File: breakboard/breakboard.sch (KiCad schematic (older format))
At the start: 2 parts

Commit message: few tracks
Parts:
- added P23, P24, P25, P48, P50, P51, P52, P81, P85, P86, P87, P88, P? (x6): CONN_1, symbol CONN_1
- gave numbers to parts that had none: 1
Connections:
- wire segments 0 -> 20
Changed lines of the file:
@@
-EESchema Schematic File Version 2  date Sun 14 Oct 2012 05:05:43 PM CEST
+EESchema Schematic File Version 2  date Tue 16 Oct 2012 02:37:21 PM CEST
 LIBS:power
 LIBS:device
@@
 LIBS:contrib
 LIBS:valves
-LIBS:motronic
+LIBS:motronic88
 LIBS:breakboard-cache
 EELAYER 25  0
@@
 Sheet 1 1
 Title ""
-Date "14 oct 2012"
+Date "16 oct 2012"
 Rev ""
 Comp ""
@@
 Comment4 ""
 $EndDescr
+Wire Wire Line
+	5100 1750 5100 1265
+Wire Wire Line
+	3950 2800 4700 2800
+Wire Wire Line
+	4700 2800 4700 1315
+Wire Wire Line
+	3950 2700 4900 2700
+Wire Wire Line
+	4900 2700 4900 1315
+Wire Wire Line
+	3950 2500 4850 2500
+Wire Wire Line
+	4850 2500 4850 1315
+Wire Wire Line
+	4750 1750 4750 1615
+Wire Wire Line
+	4250 1750 4250 1615
+Wire Wire Line
+	4050 1750 4050 1615
+Wire Wire Line
+	4150 1615 4150 1750
+Wire Wire Line
+	4350 1615 4350 1750
+Wire Wire Line
+	4800 1315 4800 2900
+Wire Wire Line
+	4800 2900 3950 2900
+Wire Wire Line
+	4650 1315 4650 2400
+Wire Wire Line
+	4650 2400 3950 2400
+Wire Wire Line
+	4750 1315 4750 1350
+Wire Wire Line
+	4750 1350 4600 1350
+Wire Wire Line
+	4600 1350 4600 2600
+Wire Wire Line
+	4600 2600 3950 2600
+$Comp
+L CONN_1 P48
+U 1 1 507D5328
+P 5100 1900
+F 0 "P48" H 5180 1900 40  0000 L CNN
+F 1 "CONN_1" H 5100 1955 30  0001 C CNN
+	1    5100 1900
+	0    1    1    0
+$EndComp
+$Comp
+L CONN_1 P81
+U 1 1 507D5152
+P 4750 1900
+F 0 "P81" H 4830 1900 40  0000 L CNN
+F 1 "CONN_1" H 4750 1955 30  0001 C CNN
+	1    4750 1900
+	0    1    1    0
+$EndComp
+$Comp
+L CONN_1 P85
+U 1 1 507D514F
+P 4350 1900
+F 0 "P85" H 4430 1900 40  0000 L CNN
+F 1 "CONN_1" H 4350 1955 30  0001 C CNN
+	1    4350 1900
+	0    1    1    0
+$EndComp
+$Comp
+L CONN_1 P?
+U 1 1 507D511B
+P 3450 2900
+F 0 "P?" H 3530 2900 40  0001 L CNN
+F 1 "CONN_1" H 3450 2955 30  0001 C CNN
+	1    3450 2900
+	1    0    0    -1
+$EndComp
+$Comp
+L CONN_1 P?
+U 1 1 507D5119
+P 3450 2800
+F 0 "P?" H 3530 2800 40  0001 L CNN
+F 1 "CONN_1" H 3450 2855 30  0001 C CNN
+	1    3450 2800
+	1    0    0    -1
+$EndComp
+$Comp
+L CONN_1 P?
+U 1 1 507D5118
+P 3450 2700
+F 0 "P?" H 3530 2700 40  0001 L CNN
+F 1 "CONN_1" H 3450 2755 30  0001 C CNN
+	1    3450 2700
+	1    0    0    -1
+$EndComp
+$Comp
+L CONN_1 P?
+U 1 1 507D5116
+P 3450 2600
+F 0 "P?" H 3530 2600 40  0001 L CNN
+F 1 "CONN_1" H 3450 2655 30  0001 C CNN
+	1    3450 2600
+	1    0    0    -1
+$EndComp
+$Comp
+L CONN_1 P51
+U 1 1 507D5114
+P 3800 2900
+F 0 "P51" H 3880 2900 40  0000 L CNN
+F 1 "CONN_1" H 3800 2955 30  0001 C CNN
+	1    3800 2900
+	-1   0    0    1
+$EndComp
+$Comp
+L CONN_1 P52
+U 1 1 507D5111
+P 3800 2800
+F 0 "P52" H 3880 2800 40  0000 L CNN
+F 1 "CONN_1" H 3800 2855 30  0001 C CNN
+	1    3800 2800
+	-1   0    0    1
+$EndComp
+$Comp
+L CONN_1 P50
+U 1 1 507D510F
+P 3800 2700
+F 0 "P50" H 3880 2700 40  0000 L CNN
+F 1 "CONN_1" H 3800 2755 30  0001 C CNN
+	1    3800 2700
+	-1   0    0    1
+$EndComp
+$Comp
+L CONN_1 P24
+U 1 1 507D510C
+P 3800 2600
+F 0 "P24" H 3880 2600 40  0000 L CNN
+F 1 "CONN_1" H 3800 2655 30  0001 C CNN
+	1    3800 2600
+	-1   0    0    1
+$EndComp
+$Comp
+L CONN_1 P23
+U 1 1 507D50D7
+P 3800 2500
+F 0 "P23" H 3880 2500 40  0000 L CNN
+F 1 "CONN_1" H 3800 2555 30  0001 C CNN
+	1    3800 2500
+	-1   0    0    1
+$EndComp
+$Comp
+L CONN_1 P?
+U 1 1 507D50D3
+P 3450 2500
+F 0 "P?" H 3530 2500 40  0001 L CNN
+F 1 "CONN_1" H 3450 2555 30  0001 C CNN
+	1    3450 2500
+	1    0    0    -1
+$EndComp
+$Comp
+L CONN_1 P25
+U 1 1 507D50C2
+P 3800 2400
+F 0 "P25" H 3880 2400 40  0000 L CNN
+F 1 "CONN_1" H 3800 2455 30  0001 C CNN
+	1    3800 2400
+	-1   0    0    1
+$EndComp
+$Comp
+L CONN_1 P?
+U 1 1 507D50BD
+P 3450 2400
+F 0 "P?" H 3530 2400 40  0001 L CNN
+F 1 "CONN_1" H 3450 2455 30  0001 C CNN
+	1    3450 2400
+	1    0    0    -1
+$EndComp
+$Comp
+L CONN_1 P86
+U 1 1 507D5092
+P 4250 1900
+F 0 "P86" H 4330 1900 40  0000 L CNN
+F 1 "CONN_1" H 4250 1955 30  0001 C CNN
+	1    4250 1900
+	0    1    1    0
+$EndComp
+$Comp
+L CONN_1 P87
+U 1 1 507D508E
+P 4150 1900
+F 0 "P87" H 4230 1900 40  0000 L CNN
+F 1 "CONN_1" H 4150 1955 30  0001 C CNN
+	1    4150 1900
+	0    1    1    0
+$EndComp
+$Comp
+L CONN_1 P88
+U 1 1 507D507A
+P 4050 1900
+F 0 "P88" H 4130 1900 40  0000 L CNN
+F 1 "CONN_1" H 4050 1955 30  0001 C CNN
+	1    4050 1900
+	0    1    1    0
+$EndComp
 $Comp
 L DB37 J?
 U 1 1 507A558A
 P 5650 7000
-F 0 "J?" H 5750 8900 70  0000 C CNN
+F 0 "J?" H 5750 8900 70  0001 C CNN
 F 1 "DB37" H 5600 5050 70  0000 C CNN
 	1    5650 7000
@@
 $EndComp
 $Comp
-L MOTRONIC88 J?
+L MOTRONIC88 J1
 U 1 1 507A5548
 P 4050 1500
-F 0 "J?" H 4130 1500 40  0000 L CNN
+F 0 "J1" H 4130 1500 40  0001 L CNN
 F 1 "MOTRONIC88" H 4050 1555 30  0001 C CNN
 	1    4050 1500

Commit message: wiring
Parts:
- removed P23, P24, P25, P50, P51, P52, P? (x6): CONN_1, symbol CONN_1
- added F1: 2A, symbol FUSE
- added F2: 20A, symbol FUSE
- added JP23, JP24, JP25, JP3, JP4, JP5, JP50, JP51, JP52: JUMPER, symbol JUMPER
- added P11, P13, P14, P16, P17, P36, P41, P44, P60, P64, P65, P73, P8: CONN_1, symbol CONN_1
- added R1, R2, R3, R4, R5, R6: 680, symbol R
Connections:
- wire segments 20 -> 103
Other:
- moved on the sheet: P48, P81, P85, P86, P87, P88

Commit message: idle board/main relay
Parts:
- added +12V, +12V?, FIDLE, ISV1, ISV2: CONN_1, symbol CONN_1
- added D? (x3): 1N4001, symbol DIODE
- added Q1, Q2, Q3, Q4, Q5, Q6: ISL9V5036P3, symbol IGBT
- added Q? (x2): IRFIZ34N, symbol MOSFET_N
- added Q? (x3): PN2222A, symbol NPN
- added R? (x2): 22, symbol R
- added R? (x3): 1k, symbol R
- added R?: 10k, symbol R
- added R? (x2): 22k, symbol R
- added R?: 4.7k, symbol R
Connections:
- net labels added: GND
- wire segments 103 -> 199
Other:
- moved on the sheet: F2

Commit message: gna
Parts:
- added D?: 1N4001, symbol DIODE
- added Q?: PN2222A, symbol NPN
- added R?: 1k, symbol R
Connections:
- net GND: now also F2.2, J1.28, J1.34, J1.43, J1.6, J1.68, J1.71, J?.1, J?.15, J?.16, J?.17, J?.18, J?.19, J?.2, Q1.3 (E), Q2.3 (E), Q3.3 (E), Q4.3 (E), Q5.3 (E), Q6.3 (E), Q?.1 (E)
- net at D?.2 (K), J1.26: now also D?.2 (K)
- net at J1.37: now also D?.1 (A), Q?.3 (C)
- net at J1.56, R?.2: now also R?.2
- net at J1.70: now also J?.23
- new net: Q?.2 (B), R?.1
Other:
- moved on the sheet: D?
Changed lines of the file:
@@
-EESchema Schematic File Version 2  date Tue 16 Oct 2012 09:22:00 PM CEST
+EESchema Schematic File Version 2  date Wed 17 Oct 2012 10:58:52 AM CEST
 LIBS:power
 LIBS:device
@@
 Sheet 1 1
 Title ""
-Date "16 oct 2012"
+Date "17 oct 2012"
 Rev ""
 Comp ""
@@
 Comment4 ""
 $EndDescr
+Connection ~ 6950 2500
+Connection ~ 6500 1000
+Wire Wire Line
+	6500 2500 6950 2500
+Wire Wire Line
+	6500 965  6500 2500
+Wire Wire Line
+	4550 6200 4550 4900
+Wire Wire Line
+	4550 4900 5850 4900
+Wire Wire Line
+	5850 4900 5850 1265
+Wire Wire Line
+	5750 1265 5750 1350
+Wire Wire Line
+	5750 1350 5650 1350
+Wire Wire Line
+	5600 1000 5650 1000
+Wire Wire Line
+	5600 1000 5600 915
+Wire Wire Line
+	4050 6200 4050 3500
+Wire Wire Line
+	4050 3500 4400 3500
+Wire Wire Line
+	4400 3500 4400 1100
+Wire Wire Line
+	4400 1100 4350 1100
+Wire Wire Line
+	4350 1100 4350 965
+Connection ~ 3850 6050
+Connection ~ 7450 5750
+Wire Wire Line
+	7600 5800 7600 5750
+Wire Wire Line
+	7600 5750 6650 5750
+Connection ~ 7250 1500
+Wire Wire Line
+	7250 1500 7900 1500
+Wire Wire Line
+	7900 1500 7900 1550
+Wire Wire Line
+	7600 2100 7600 2000
+Wire Wire Line
+	7600 2000 6550 2000
+Wire Wire Line
+	6550 2000 6550 1050
+Connection ~ 6200 1050
+Wire Wire Line
+	6550 1050 6200 1050
+Wire Wire Line
+	6200 1600 5300 1600
+Wire Wire Line
+	5300 1600 5300 1100
+Wire Wire Line
+	5300 1100 4550 1100
+Wire Wire Line
+	4450 1500 4550 1500
+Wire Wire Line
+	4450 1500 4450 965
 Wire Wire Line
 	5550 5200 5550 2800
@@
 Wire Wire Line
 	7250 1550 7250 1265
-Wire Wire Line
-	4550 1050 4550 965
 Connection ~ 11000 1400
 Wire Wire Line
@@
 Connection ~ 6850 5750
 Wire Wire Line
-	6650 5750 7450 5750
-Wire Wire Line
 	6650 5750 6650 6200
 Connection ~ 7250 5750
@@
 Connection ~ 1250 3000
 Wire Wire Line
-	1250 6000 1250 1000
-Wire Wire Line
 	1250 6000 1500 6000
 Connection ~ 1250 5000
 Wire Wire Line
-	1250 1000 2000 1000
+	2000 1000 1250 1000
 Wire Wire Line
 	10450 2200 10500 2200
@@
 Connection ~ 9650 1350
 Wire Wire Line
-	4450 965  4450 1450
-Wire Wire Line
-	4450 1450 4550 1450
-Wire Wire Line
 	6950 1265 6950 1900
 Wire Wire Line
@@
 	7250 2300 7250 2050
 Wire Wire Line
-	4550 1450 4550 2100
-Wire Wire Line
-	4550 2100 6950 2100
+	6950 2100 4550 2100
 Wire Wire Line
 	5450 2750 7900 2750
@@
 Wire Wire Line
 	4950 4000 4950 6200
+Wire Wire Line
+	4550 1100 4550 965
+Wire Wire Line
+	4550 2100 4550 1500
+Wire Wire Line
+	6200 1200 6200 915
+Wire Wire Line
+	7900 2050 7900 2300
+Wire Wire Line
+	7600 2500 7600 2550
+Wire Wire Line
+	1250 1000 1250 6650
+Connection ~ 1250 6000
+Wire Wire Line
+	3550 6250 3550 6050
+Wire Wire Line
+	3550 6050 4050 6050
+Connection ~ 4050 6050
+Wire Wire Line
+	5650 1000 5650 2450
+Wire Wire Line
+	5650 2450 4400 2450
+Connection ~ 4400 2450
+Connection ~ 5650 1350
+Wire Wire Line
+	6500 1000 6550 1000
+Wire Wire Line
+	6550 1000 6550 965
+$Comp
+L GND #PWR?
+U 1 1 507E71C0
+P 3550 6250
+F 0 "#PWR?" H 3550 6250 30  0001 C CNN
+F 1 "GND" H 3550 6180 30  0001 C CNN
+	1    3550 6250
+	1    0    0    -1
+$EndComp
+$Comp
+L GND #PWR?
+U 1 1 507E71BB
+P 1250 6650
+F 0 "#PWR?" H 1250 6650 30  0001 C CNN
+F 1 "GND" H 1250 6580 30  0001 C CNN
+	1    1250 6650
+	1    0    0    -1
+$EndComp
+$Comp
+L GND #PWR?
+U 1 1 507E71AA
+P 7600 5800
+F 0 "#PWR?" H 7600 5800 30  0001 C CNN
+F 1 "GND" H 7600 5730 30  0001 C CNN
+	1    7600 5800
+	1    0    0    -1
+$EndComp
+$Comp
+L DIODE D?
+U 1 1 507E6EB8
+P 6200 1400
+F 0 "D?" H 6200 1500 40  0000 C CNN
+F 1 "1N4001" H 6200 1300 40  0000 C CNN
+	1    6200 1400
+	0    -1   1    0
+$EndComp
+$Comp
+L R R?
+U 1 1 507E6DD7
+P 7900 1800
+F 0 "R?" V 7980 1800 50  0000 C CNN
+F 1 "1k" V 7900 1800 50  0000 C CNN
+	1    7900 1800
+	-1   0    0    1
+$EndComp
+$Comp
+L GND #PWR?
+U 1 1 507E6DCF
+P 7600 2550
+F 0 "#PWR?" H 7600 2550 30  0001 C CNN
+F 1 "GND" H 7600 2480 30  0001 C CNN
+	1    7600 2550
+	1    0    0    -1
+$EndComp
+$Comp
+L NPN Q?
+U 1 1 507E6DC7
+P 7700 2300
+F 0 "Q?" H 7700 2150 50  0000 R CNN
+F 1 "PN2222A" H 7700 2450 50  0000 R CNN
+	1    7700 2300
+	-1   0    0    -1
+$EndComp
 $Comp
 L R R?
@@
 L DIODE D?
 U 1 1 507DAE65
-P 4550 1250
-F 0 "D?" H 4550 1350 40  0000 C CNN
-F 1 "1N4001" H 4550 1150 40  0000 C CNN
-	1    4550 1250
+P 4550 1300
+F 0 "D?" H 4550 1400 40  0000 C CNN
+F 1 "1N4001" H 4550 1200 40  0000 C CNN
+	1    4550 1300
 	0    -1   -1   0
 $EndComp

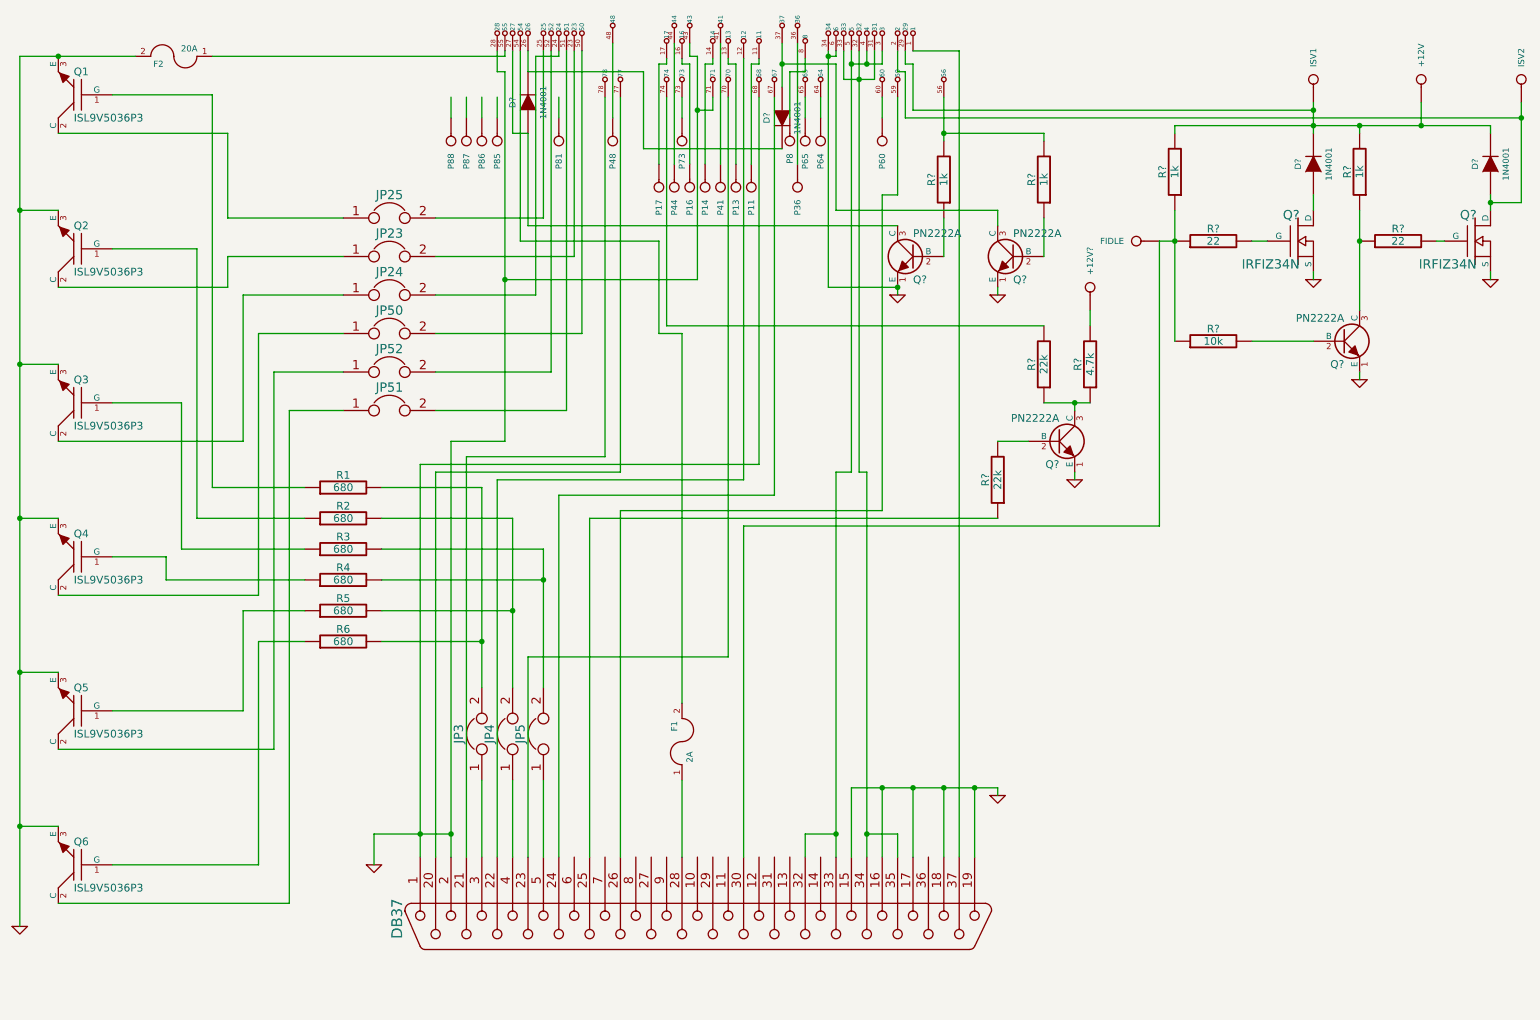
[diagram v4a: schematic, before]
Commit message: new components in the db + first layouts
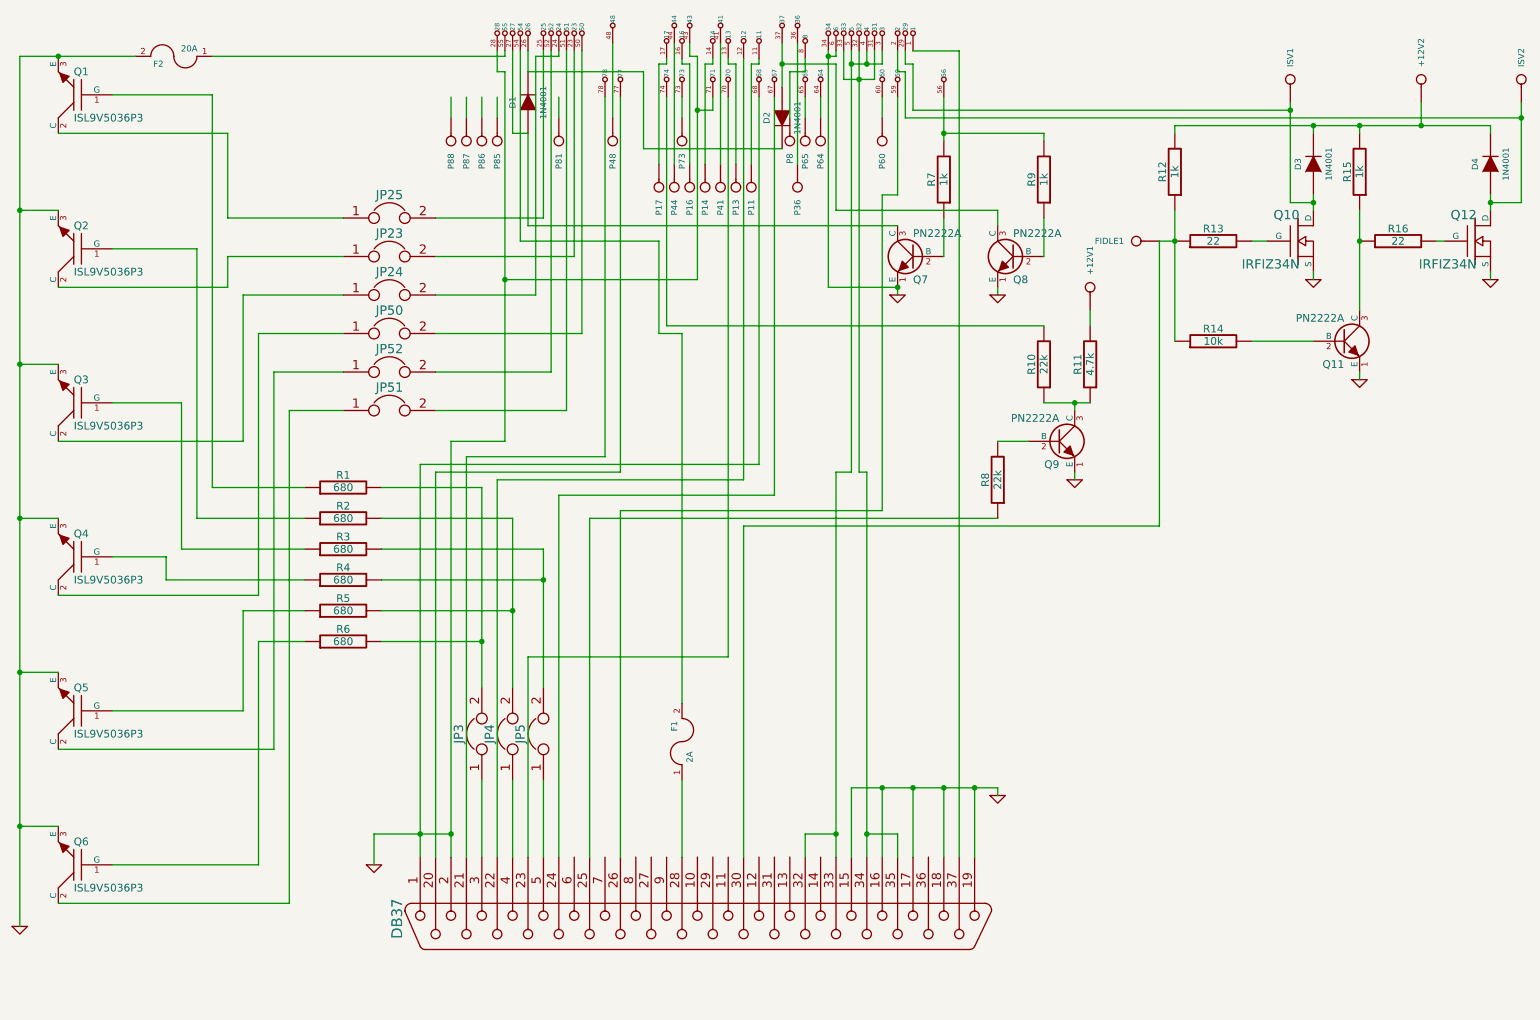
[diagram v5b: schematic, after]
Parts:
- gave numbers to parts that had none: 22
- renumbered +12V to +12V2, FIDLE to FIDLE1
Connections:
- net at +12V2.1, D3.2 (K), D4.2 (K)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: no longer ISV1.1, J1.29
- net at D3.1 (A), Q10.D: now also ISV1.1, J1.29
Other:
- moved on the sheet: ISV1

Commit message: new ignition layout
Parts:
- removed JP23, JP24, JP25, JP50, JP51, JP52: JUMPER, symbol JUMPER
- removed P81, P85, P86, P87, P88: CONN_1, symbol CONN_1
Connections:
- net at J1.23: now also Q2.2 (C)
- net at J1.24: now also Q3.2 (C)
- net at J1.25: now also Q1.2 (C)
- net at J1.50: now also Q4.2 (C)
- net at J1.51: now also Q6.2 (C)
- net at J1.52: now also Q5.2 (C)
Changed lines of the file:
@@
-EESchema Schematic File Version 2  date Sat 20 Oct 2012 05:10:12 PM CEST
+EESchema Schematic File Version 2  date Mon 22 Oct 2012 02:06:11 PM CEST
 LIBS:power
 LIBS:device
@@
 Sheet 1 1
 Title ""
-Date "20 oct 2012"
+Date "22 oct 2012"
 Rev ""
 Comp ""
@@
 Comment4 ""
 $EndDescr
+Wire Wire Line
+	3000 3300 4800 3300
+Wire Wire Line
+	2800 2800 4900 2800
+Wire Wire Line
+	2600 2300 4850 2300
 Connection ~ 9500 1350
 Wire Wire Line
@@
 	2600 2500 2600 2300
 Wire Wire Line
-	2600 2300 3350 2300
-Wire Wire Line
 	3100 4200 2300 4200
 Wire Wire Line
@@
 	2800 6250 1850 6250
 Wire Wire Line
-	3350 2800 2800 2800
-Wire Wire Line
 	2800 2800 2800 4500
 Wire Wire Line
 	2800 4500 1500 4500
-Wire Wire Line
-	3350 3300 3000 3300
 Wire Wire Line
 	3000 3300 3000 6500
@@
 	4250 3800 3600 3800
 Wire Wire Line
-	3950 2550 4600 2550
-Wire Wire Line
-	4600 2550 4600 1000
-Wire Wire Line
-	3950 3050 4700 3050
-Wire Wire Line
-	3950 3300 4800 3300
+	4600 1000 4600 2550
 Wire Wire Line
 	4800 3300 4800 965
@@
 	5100 1400 5100 915
 Wire Wire Line
-	4750 1400 4750 1265
-Wire Wire Line
-	4250 1400 4250 1265
-Wire Wire Line
-	4050 1400 4050 1265
-Wire Wire Line
-	4150 1265 4150 1400
-Wire Wire Line
-	4350 1265 4350 1400
-Wire Wire Line
 	4650 965  4650 2050
 Wire Wire Line
-	4650 2050 3950 2050
-Wire Wire Line
 	4750 965  4750 1000
 Wire Wire Line
@@
 	4250 6200 4250 5700
 Wire Wire Line
-	4700 3050 4700 965
-Wire Wire Line
-	4900 965  4900 2800
-Wire Wire Line
-	4900 2800 3950 2800
-Wire Wire Line
-	4850 965  4850 2300
-Wire Wire Line
-	4850 2300 3950 2300
+	4700 965  4700 3050
+Wire Wire Line
+	4900 2800 4900 965
+Wire Wire Line
+	4850 2300 4850 965
 Wire Wire Line
 	3600 4800 4250 4800
@@
 	2900 5500 2900 3050
 Wire Wire Line
-	2900 3050 3350 3050
-Wire Wire Line
 	1500 3500 2700 3500
 Wire Wire Line
 	2700 3500 2700 2550
 Wire Wire Line
-	2700 2550 3350 2550
-Wire Wire Line
-	3350 2050 2600 2050
-Wire Wire Line
-	2600 2050 2600 1500
+	2600 1500 2600 2050
 Wire Wire Line
 	2600 1500 1500 1500
@@
 	9500 1950 9650 1950
 Connection ~ 9650 1950
+Wire Wire Line
+	2600 2050 4650 2050
+Wire Wire Line
+	2700 2550 4600 2550
+Wire Wire Line
+	2900 3050 4700 3050
 $Comp
 L GND #PWR01
@@
 $EndComp
 $Comp
-L JUMPER JP51
-U 1 1 507D5D5B
-P 3650 3300
-F 0 "JP51" H 3650 3450 60  0000 C CNN
-F 1 "JUMPER" H 3650 3220 40  0001 C CNN
-	1    3650 3300
-	1    0    0    -1
-$EndComp
-$Comp
-L JUMPER JP52
-U 1 1 507D5D57
-P 3650 3050
-F 0 "JP52" H 3650 3200 60  0000 C CNN
-F 1 "JUMPER" H 3650 2970 40  0001 C CNN
-	1    3650 3050
-	1    0    0    -1
-$EndComp
-$Comp
-L JUMPER JP50
-U 1 1 507D5D50
-P 3650 2800
-F 0 "JP50" H 3650 2950 60  0000 C CNN
-F 1 "JUMPER" H 3650 2720 40  0001 C CNN
-	1    3650 2800
-	1    0    0    -1
-$EndComp
-$Comp
-L JUMPER JP24
-U 1 1 507D5D44
-P 3650 2550
-F 0 "JP24" H 3650 2700 60  0000 C CNN
-F 1 "JUMPER" H 3650 2470 40  0001 C CNN
-	1    3650 2550
-	1    0    0    -1
-$EndComp
-$Comp
-L JUMPER JP23
-U 1 1 507D5D0C
-P 3650 2300
-F 0 "JP23" H 3650 2450 60  0000 C CNN
-F 1 "JUMPER" H 3650 2220 40  0001 C CNN
-	1    3650 2300
-	1    0    0    -1
-$EndComp
-$Comp
-L JUMPER JP25
-U 1 1 507D5CDB
-P 3650 2050
-F 0 "JP25" H 3650 2200 60  0000 C CNN
-F 1 "JUMPER" H 3650 1970 40  0001 C CNN
-	1    3650 2050
-	1    0    0    -1
-$EndComp
-$Comp
 L JUMPER JP5
 U 1 1 507D5C40
@@
 	0    1    1    0
 $EndComp
-$Comp
-L CONN_1 P81
-U 1 1 507D5152
-P 4750 1550
-F 0 "P81" H 4830 1550 40  0000 L CNN
-F 1 "CONN_1" H 4750 1605 30  0001 C CNN
-	1    4750 1550
-	0    1    1    0
-$EndComp
-$Comp
-L CONN_1 P85
-U 1 1 507D514F
-P 4350 1550
-F 0 "P85" H 4430 1550 40  0000 L CNN
-F 1 "CONN_1" H 4350 1605 30  0001 C CNN
-	1    4350 1550
-	0    1    1    0
-$EndComp
-$Comp
-L CONN_1 P86
-U 1 1 507D5092
-P 4250 1550
-F 0 "P86" H 4330 1550 40  0000 L CNN
-F 1 "CONN_1" H 4250 1605 30  0001 C CNN
-	1    4250 1550
-	0    1    1    0
-$EndComp
-$Comp
-L CONN_1 P87
-U 1 1 507D508E
-P 4150 1550
-F 0 "P87" H 4230 1550 40  0000 L CNN
-F 1 "CONN_1" H 4150 1605 30  0001 C CNN
-	1    4150 1550
-	0    1    1    0
-$EndComp
-$Comp
-L CONN_1 P88
-U 1 1 507D507A
-P 4050 1550
-F 0 "P88" H 4130 1550 40  0000 L CNN
-F 1 "CONN_1" H 4050 1605 30  0001 C CNN
-	1    4050 1550
-	0    1    1    0
-$EndComp
